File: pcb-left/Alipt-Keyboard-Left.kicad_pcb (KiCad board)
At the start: 2 copper layers, 197.4 x 119.6 mm, 83 parts, among them J1 LED, J2 4PIN, J3 OLED, P1 i2c_pin, P2 i2c_pin, SW0 SW_PUSH, SW1 SW_PUSH, SW10 SW_PUSH, SW11 SW_PUSH, SW12 SW_PUSH, SW13 SW_PUSH, SW14 SW_PUSH, SW15 SW_PUSH, SW16 SW_PUSH, SW17 SW_PUSH, SW18 SW_PUSH, SW19 SW_PUSH, SW2 SW_PUSH, SW20 SW_PUSH, SW21 SW_PUSH, SW22 SW_PUSH, SW23 SW_PUSH, SW24 SW_PUSH, SW25 SW_PUSH, SW26 SW_PUSH, SW27 SW_PUSH, SW28 SW_PUSH, SW29 SW_PUSH, SW3 SW_PUSH, SW30 SW_PUSH, SW31 SW_PUSH, SW32 Rotary_Encoder_Switch, SW4 SW_PUSH, SW5 SW_PUSH, SW6 SW_PUSH, SW7 SW_PUSH, SW8 SW_PUSH, SW9 SW_PUSH, U1 ProMicro

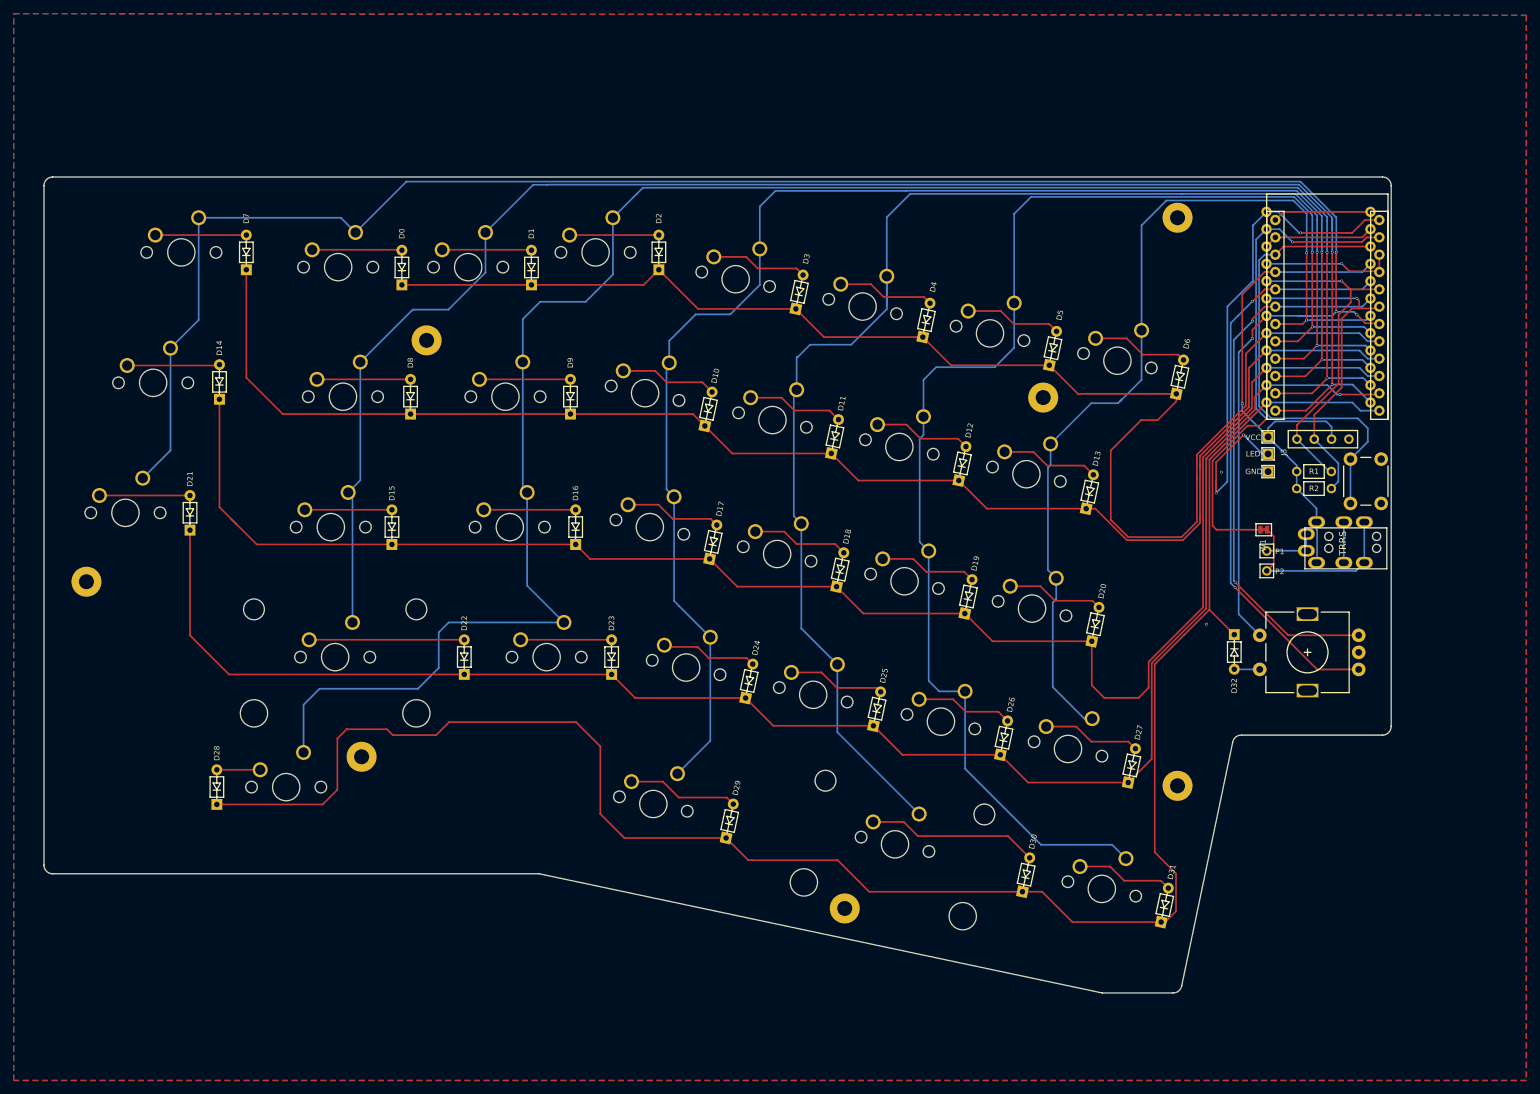
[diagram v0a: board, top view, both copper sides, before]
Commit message: Revision 2 PCB Changes
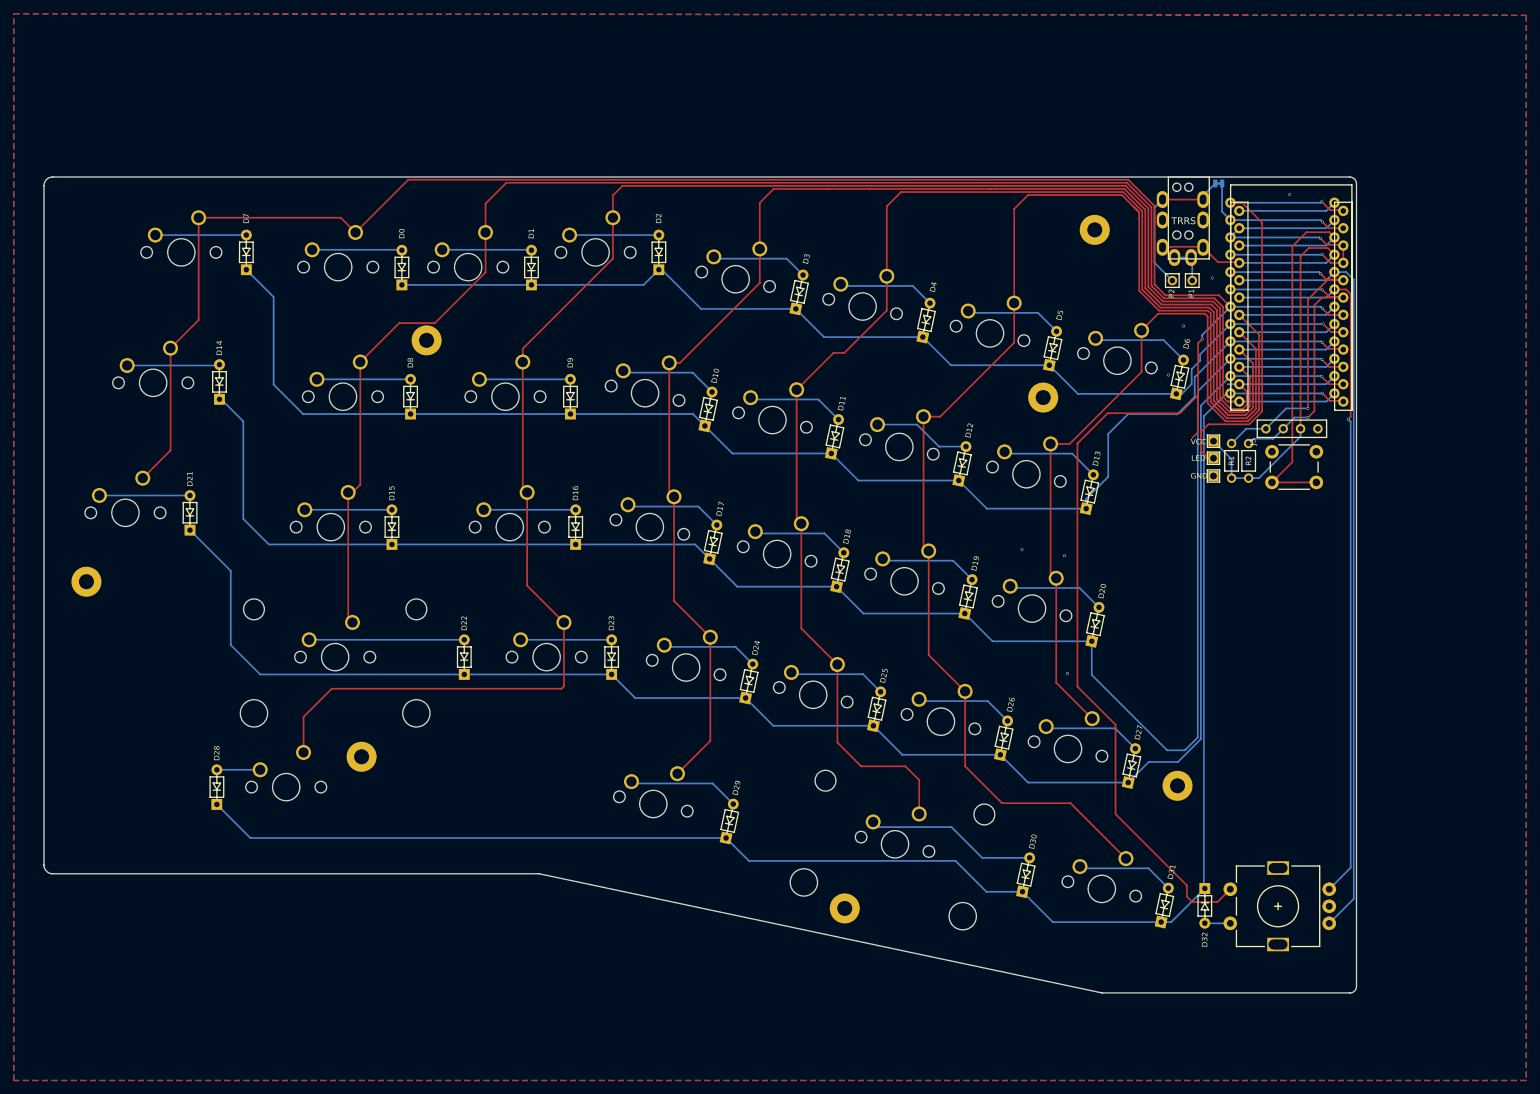
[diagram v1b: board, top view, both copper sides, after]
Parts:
- W1: moved to B.Cu
- moved J2 61.7 mm to (202.1, 43.2), turned to 0 degrees
- moved W1 51.2 mm to (206.4, 44.1), turned to 180 degrees
- moved P2 44.7 mm to (199.6, 58.4), turned to 270 degrees
- moved P1 41.1 mm to (202.6, 58.4), turned to 270 degrees
- moved D32 37.5 mm to (204.4, 146.2)
- moved SW32 37.5 mm to (215.1, 150.1)
- moved RSW1 16.0 mm to (214.2, 83.4), turned to 0 degrees
- moved TH1 12.3 mm to (188.3, 50.9)
- moved R1 12.2 mm to (208.3, 84.8), turned to 90 degrees
- moved R2 10.4 mm to (210.8, 84.8), turned to 90 degrees
- moved J1 8.03 mm to (205.7, 81.9)
- moved U1 5.45 mm to (217.0, 61.7)
- moved J3 4.79 mm to (213.4, 80.1)
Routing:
- net row0: track 209.5 -> 153.0 mm, vias 0 -> 1
- net SW32A: track 298.4 -> 351.0 mm, vias 4 -> 2
- net DATA: track 73.9 -> 22.9 mm, vias 2 -> 1
- net row4: track 274.2 -> 245.6 mm, vias 0 -> 1
- net ENCA: track 85.1 -> 113.5 mm, vias 2 -> 0
- net ENCB: track 79.7 -> 105.9 mm, vias 2 -> 1
- net LED: track 79.7 -> 65.9 mm, vias 3 -> 1
- net row1: track 213.2 -> 199.6 mm, vias 0 -> 1
- net col0: track 141.1 -> 129.1 mm, vias 2 -> 0
- net col5: track 240.6 -> 229.2 mm, vias 2 -> 0
- net row2: track 240.0 -> 251.2 mm, vias 0 -> 1
- net GND: track 44.4 -> 55.5 mm, vias 3 -> 9
- net col1: track 203.5 -> 212.8 mm, vias 2 -> 0
- net /i2c_d: track 27.6 -> 22.5 mm
- net col4: track 271.6 -> 266.6 mm, vias 2 -> 0
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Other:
- board size 197.4 x 119.6 mm -> 192.3 x 119.6 mm
